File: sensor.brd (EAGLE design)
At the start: 30.5 x 35.6 mm, 17 parts, among them IC1 TINY261A

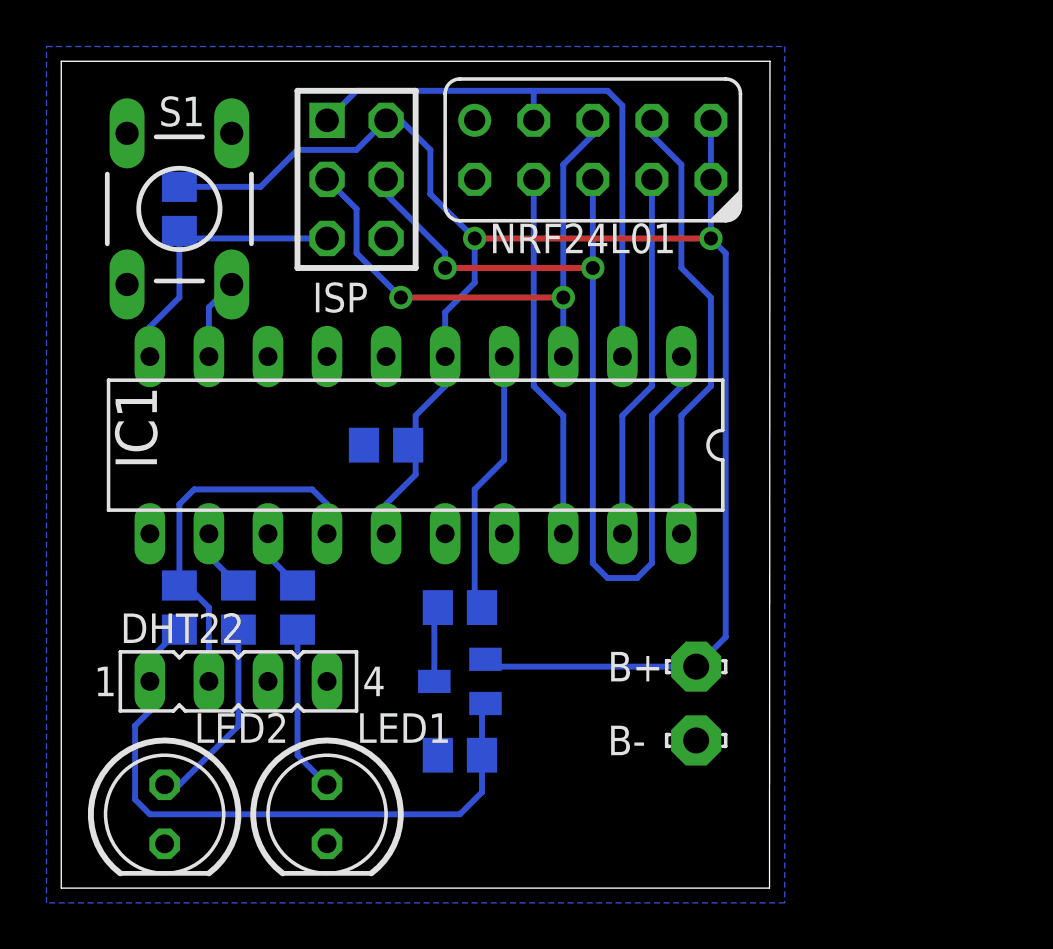
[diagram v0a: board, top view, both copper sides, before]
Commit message: added watch crystal to master, notes for sensor
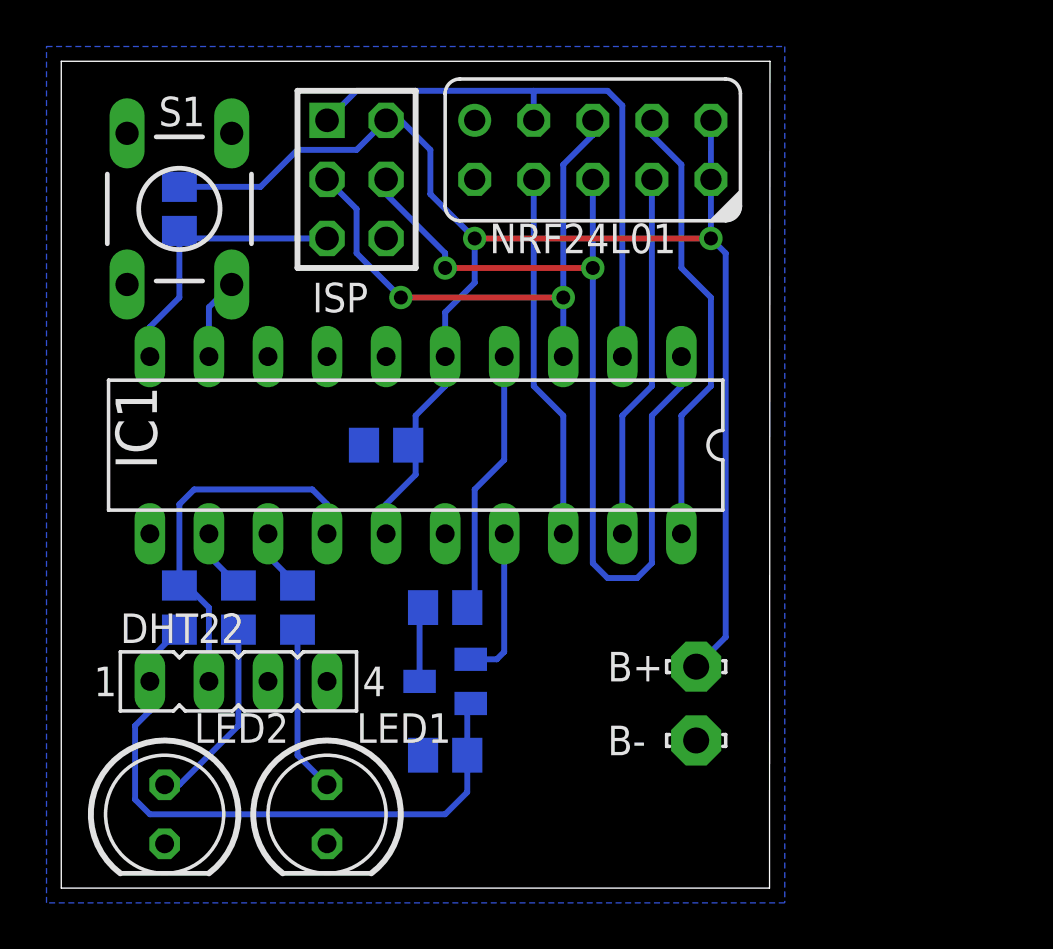
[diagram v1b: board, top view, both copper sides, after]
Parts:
- moved C2 0.63 mm to (16.5, 5.71)
- moved C3 0.63 mm to (16.5, 12.1)
- moved D1 0.63 mm to (16.5, 8.89)
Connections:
- new net PA3: D1.1, IC1.17
- net VCC: no longer D1.1
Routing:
- net VCC: track 75.3 -> 66.1 mm
- net PA3: track 0.00 -> 6.65 mm
- net DHTVCC: track 27.5 -> 26.9 mm
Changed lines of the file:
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@@
 <layer number="22" name="bPlace" color="7" fill="1" visible="yes" active="yes"/>
 <layer number="23" name="tOrigins" color="15" fill="1" visible="no" active="yes"/>
-<layer number="24" name="bOrigins" color="15" fill="1" visible="no" active="yes"/>
+<layer number="24" name="bOrigins" color="15" fill="1" visible="yes" active="yes"/>
 <layer number="25" name="tNames" color="7" fill="1" visible="yes" active="yes"/>
 <layer number="26" name="bNames" color="7" fill="1" visible="yes" active="yes"/>
@@
 <attribute name="VALUE" x="15.24" y="16.51" size="1.27" layer="28" rot="MR0"/>
 </element>
-<element name="C2" library="rcl" package="C0805" value="100n" x="17.145" y="5.715" smashed="yes" rot="MR180">
-<attribute name="NAME" x="19.05" y="6.35" size="1.27" layer="26" rot="MR180"/>
-<attribute name="VALUE" x="15.875" y="8.255" size="1.27" layer="28" rot="MR180"/>
+<element name="C2" library="rcl" package="C0805" value="100n" x="16.51" y="5.715" smashed="yes" rot="MR180">
+<attribute name="NAME" x="18.415" y="6.35" size="1.27" layer="26" rot="MR180"/>
+<attribute name="VALUE" x="15.24" y="8.255" size="1.27" layer="28" rot="MR180"/>
 </element>
 <element name="DHT22" library="con-lsta" package="FE04-1" value="" x="7.62" y="8.89"/>
 <element name="R2" library="rcl" package="R0805" value="10k" x="5.08" y="12.065" smashed="yes" rot="MR90">
-<attribute name="NAME" x="12.573" y="13.335" size="1.27" layer="26" rot="MR270"/>
+<attribute name="NAME" x="3.683" y="13.335" size="1.27" layer="26" rot="MR270"/>
 <attribute name="VALUE" x="2.54" y="11.43" size="1.27" layer="28" rot="MR90"/>
 </element>
@@
 <attribute name="VALUE" x="25.4" y="19.812" size="1.778" layer="27" ratio="10" rot="R180"/>
 </element>
-<element name="D1" library="diode" package="SOT23" value="BAT54S" x="17.145" y="8.89" smashed="yes" rot="MR270">
-<attribute name="NAME" x="19.05" y="8.89" size="1.27" layer="26" rot="MR180"/>
-<attribute name="VALUE" x="20.32" y="10.795" size="1.27" layer="28" rot="MR270"/>
-</element>
-<element name="C3" library="rcl" package="C0805" value="100n" x="17.145" y="12.065" smashed="yes" rot="MR0">
-<attribute name="NAME" x="19.05" y="12.7" size="1.27" layer="26" rot="MR180"/>
-<attribute name="VALUE" x="18.415" y="9.525" size="1.27" layer="28" rot="MR0"/>
+<element name="D1" library="diode" package="SOT23" value="BAT54S" x="16.51" y="8.89" smashed="yes" rot="MR270">
+<attribute name="NAME" x="18.415" y="8.89" size="1.27" layer="26" rot="MR180"/>
+<attribute name="VALUE" x="19.685" y="10.795" size="1.27" layer="28" rot="MR270"/>
+</element>
+<element name="C3" library="rcl" package="C0805" value="100n" x="16.51" y="12.065" smashed="yes" rot="MR0">
+<attribute name="NAME" x="18.415" y="12.7" size="1.27" layer="26" rot="MR180"/>
+<attribute name="VALUE" x="17.78" y="9.525" size="1.27" layer="28" rot="MR0"/>
 </element>
 <element name="R3" library="rcl" package="R0805" value="510" x="10.16" y="12.065" smashed="yes" rot="MR270">
-<attribute name="NAME" x="14.986" y="13.335" size="1.27" layer="26" rot="MR270"/>
+<attribute name="NAME" x="13.97" y="13.335" size="1.27" layer="26" rot="MR270"/>
 <attribute name="VALUE" x="12.7" y="12.7" size="1.27" layer="28" rot="MR270"/>
 </element>
@@
 </element>
 <element name="R4" library="rcl" package="R0805" value="470" x="7.62" y="12.065" smashed="yes" rot="MR270">
-<attribute name="NAME" x="13.716" y="13.335" size="1.27" layer="26" rot="MR270"/>
+<attribute name="NAME" x="12.7" y="13.335" size="1.27" layer="26" rot="MR270"/>
 <attribute name="VALUE" x="10.16" y="12.7" size="1.27" layer="28" rot="MR270"/>
 </element>
@@
 <contactref element="C1" pad="1"/>
 <wire x1="27.94" y1="30.48" x2="27.94" y2="33.02" width="0.254" layer="16"/>
-<contactref element="D1" pad="1"/>
 <wire x1="16.51" y1="22.86" x2="16.51" y2="24.765" width="0.254" layer="16"/>
 <wire x1="16.51" y1="24.765" x2="17.78" y2="26.035" width="0.254" layer="16"/>
@@
 <wire x1="27.94" y1="27.94" x2="28.575" y2="27.305" width="0.254" layer="16"/>
 <wire x1="28.575" y1="27.305" x2="28.575" y2="10.795" width="0.254" layer="16"/>
-<wire x1="27.305" y1="9.525" x2="18.56" y2="9.525" width="0.254" layer="16"/>
-<wire x1="18.56" y1="9.525" x2="18.245" y2="9.84" width="0.254" layer="16"/>
 <wire x1="28.575" y1="10.795" x2="27.305" y2="9.525" width="0.254" layer="16"/>
 <wire x1="15.24" y1="17.78" x2="13.97" y2="16.51" width="0.254" layer="16"/>
@@
 <wire x1="19.05" y1="22.86" x2="19.05" y2="18.415" width="0.254" layer="16"/>
 <wire x1="19.05" y1="18.415" x2="17.78" y2="17.145" width="0.254" layer="16"/>
-<wire x1="17.78" y1="17.145" x2="17.78" y2="12.38" width="0.254" layer="16"/>
-<wire x1="17.78" y1="12.38" x2="18.095" y2="12.065" width="0.254" layer="16"/>
+<wire x1="17.145" y1="12.38" x2="17.46" y2="12.065" width="0.254" layer="16"/>
+<wire x1="17.78" y1="17.145" x2="17.78" y2="12.385" width="0.254" layer="16"/>
+<wire x1="17.78" y1="12.385" x2="17.46" y2="12.065" width="0.254" layer="16"/>
 </signal>
 <signal name="PA2">
@@
 <contactref element="C3" pad="2"/>
 <contactref element="D1" pad="3"/>
-<wire x1="16.045" y1="8.89" x2="16.045" y2="11.915" width="0.254" layer="16"/>
-<wire x1="16.045" y1="11.915" x2="16.195" y2="12.065" width="0.254" layer="16"/>
+<wire x1="15.41" y1="8.89" x2="15.41" y2="11.915" width="0.254" layer="16"/>
+<wire x1="15.41" y1="11.915" x2="15.56" y2="12.065" width="0.254" layer="16"/>
 </signal>
 <signal name="DHTVCC">
@@
 <contactref element="C2" pad="2"/>
 <contactref element="R2" pad="1"/>
-<wire x1="18.095" y1="7.79" x2="18.245" y2="7.94" width="0.254" layer="16"/>
-<wire x1="18.095" y1="7.79" x2="18.095" y2="5.715" width="0.254" layer="16"/>
+<wire x1="17.46" y1="7.79" x2="17.61" y2="7.94" width="0.254" layer="16"/>
+<wire x1="17.46" y1="7.79" x2="17.46" y2="5.715" width="0.254" layer="16"/>
 <wire x1="3.81" y1="8.89" x2="3.81" y2="7.62" width="0.254" layer="16"/>
 <wire x1="3.81" y1="8.89" x2="3.81" y2="9.845" width="0.254" layer="16"/>
 <wire x1="3.81" y1="9.845" x2="5.08" y2="11.115" width="0.254" layer="16"/>
-<wire x1="18.095" y1="5.715" x2="18.095" y2="4.125" width="0.254" layer="16"/>
-<wire x1="18.095" y1="4.125" x2="17.145" y2="3.175" width="0.254" layer="16"/>
-<wire x1="17.145" y1="3.175" x2="3.81" y2="3.175" width="0.254" layer="16"/>
+<wire x1="17.46" y1="5.715" x2="17.46" y2="4.125" width="0.254" layer="16"/>
+<wire x1="17.46" y1="4.125" x2="16.51" y2="3.175" width="0.254" layer="16"/>
+<wire x1="16.51" y1="3.175" x2="3.81" y2="3.175" width="0.254" layer="16"/>
 <wire x1="3.81" y1="3.175" x2="3.175" y2="3.81" width="0.254" layer="16"/>
 <wire x1="3.175" y1="3.81" x2="3.175" y2="6.985" width="0.254" layer="16"/>
@@
 <wire x1="10.16" y1="5.715" x2="10.16" y2="11.115" width="0.254" layer="16"/>
 </signal>
+<signal name="PA3">
+<contactref element="IC1" pad="17"/>
+<contactref element="D1" pad="1"/>
+<wire x1="19.05" y1="15.24" x2="19.05" y2="10.16" width="0.254" layer="16"/>
+<wire x1="19.05" y1="10.16" x2="18.73" y2="9.84" width="0.254" layer="16"/>
+<wire x1="18.73" y1="9.84" x2="17.61" y2="9.84" width="0.254" layer="16"/>
+</signal>
 </signals>

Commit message: di == miso, do == mosi for usi in spi mode
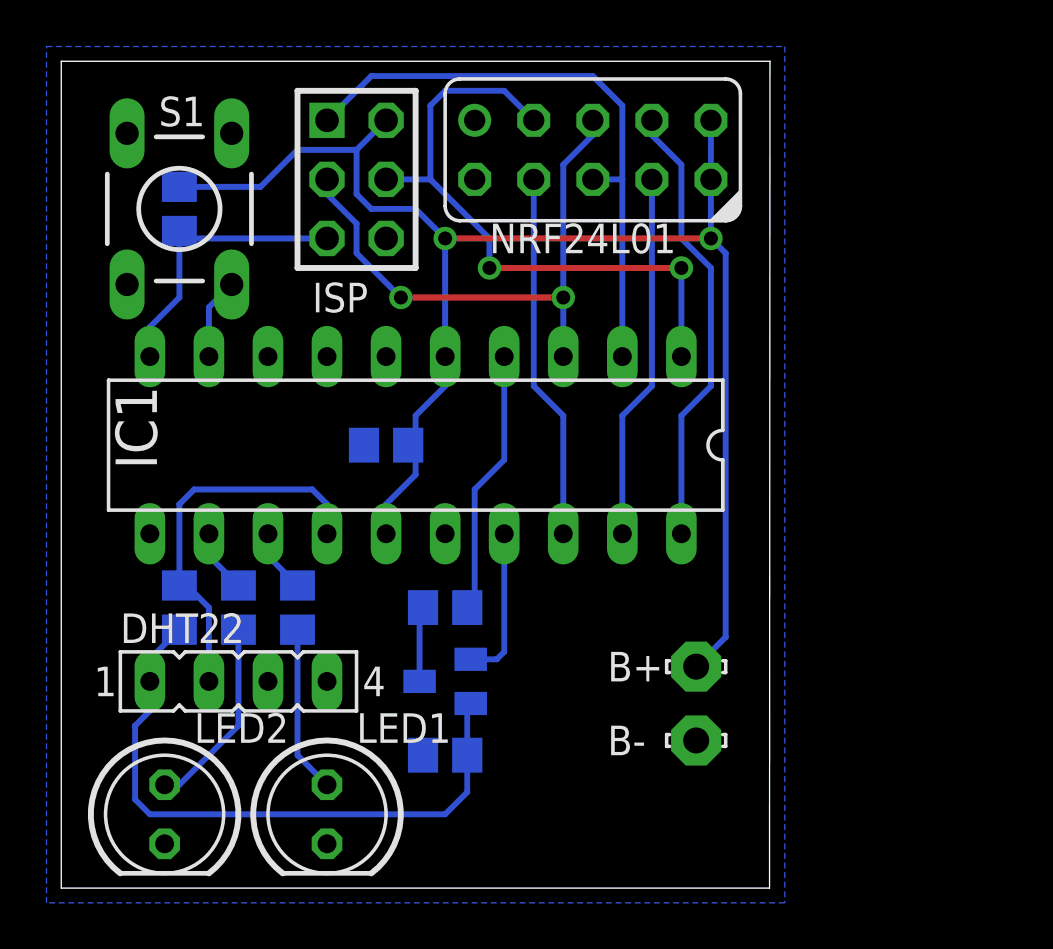
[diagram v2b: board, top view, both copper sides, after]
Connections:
- net PB0: now also NRF24L01.3; no longer NRF24L01.6
- net PB1: now also NRF24L01.6; no longer NRF24L01.3
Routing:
- net PB0: track 40.2 -> 27.2 mm
- net PB1: track 25.6 -> 26.1 mm
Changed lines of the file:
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@@
 <contactref element="C1" pad="1"/>
 <wire x1="27.94" y1="30.48" x2="27.94" y2="33.02" width="0.254" layer="16"/>
-<wire x1="16.51" y1="22.86" x2="16.51" y2="24.765" width="0.254" layer="16"/>
-<wire x1="16.51" y1="24.765" x2="17.78" y2="26.035" width="0.254" layer="16"/>
-<wire x1="17.78" y1="26.035" x2="17.78" y2="27.94" width="0.254" layer="16"/>
-<wire x1="17.78" y1="27.94" x2="15.875" y2="29.845" width="0.254" layer="16"/>
-<wire x1="15.875" y1="29.845" x2="15.875" y2="31.75" width="0.254" layer="16"/>
-<wire x1="15.875" y1="31.75" x2="14.605" y2="33.02" width="0.254" layer="16"/>
-<wire x1="14.605" y1="33.02" x2="13.97" y2="33.02" width="0.254" layer="16"/>
+<wire x1="16.51" y1="22.86" x2="16.51" y2="27.94" width="0.254" layer="16"/>
+<wire x1="12.7" y1="29.845" x2="12.7" y2="31.75" width="0.254" layer="16"/>
 <wire x1="5.08" y1="30.16" x2="8.57" y2="30.16" width="0.254" layer="16"/>
 <wire x1="8.57" y1="30.16" x2="10.16" y2="31.75" width="0.254" layer="16"/>
@@
 <wire x1="16.51" y1="21.59" x2="16.51" y2="22.86" width="0.254" layer="16"/>
 <wire x1="13.97" y1="15.24" x2="13.97" y2="16.51" width="0.254" layer="16"/>
-<via x="17.78" y="27.94" extent="1-16" drill="0.6"/>
-<wire x1="17.78" y1="27.94" x2="27.94" y2="27.94" width="0.254" layer="1"/>
+<via x="16.51" y="27.94" extent="1-16" drill="0.6"/>
+<wire x1="16.51" y1="27.94" x2="27.94" y2="27.94" width="0.254" layer="1"/>
 <via x="27.94" y="27.94" extent="1-16" drill="0.6"/>
 <wire x1="27.94" y1="27.94" x2="27.94" y2="30.48" width="0.254" layer="16"/>
@@
 <wire x1="15.24" y1="20.32" x2="15.24" y2="19.37" width="0.254" layer="16"/>
 <wire x1="15.24" y1="19.37" x2="14.92" y2="19.05" width="0.254" layer="16"/>
+<wire x1="12.7" y1="29.845" x2="13.335" y2="29.21" width="0.254" layer="16"/>
+<wire x1="13.335" y1="29.21" x2="15.24" y2="29.21" width="0.254" layer="16"/>
+<wire x1="15.24" y1="29.21" x2="16.51" y2="27.94" width="0.254" layer="16"/>
 </signal>
 <signal name="PA4">
@@
 </signal>
 <signal name="PB0">
-<contactref element="NRF24L01" pad="6"/>
 <contactref element="ISP" pad="4"/>
 <contactref element="IC1" pad="1"/>
-<wire x1="13.97" y1="30.48" x2="13.97" y2="29.845" width="0.254" layer="16"/>
-<wire x1="13.97" y1="29.845" x2="16.51" y2="27.305" width="0.254" layer="16"/>
-<wire x1="16.51" y1="27.305" x2="16.51" y2="26.67" width="0.254" layer="16"/>
-<wire x1="26.67" y1="22.86" x2="26.67" y2="21.59" width="0.254" layer="16"/>
-<wire x1="26.67" y1="21.59" x2="25.4" y2="20.32" width="0.254" layer="16"/>
-<wire x1="25.4" y1="20.32" x2="25.4" y2="13.97" width="0.254" layer="16"/>
-<wire x1="25.4" y1="13.97" x2="24.765" y2="13.335" width="0.254" layer="16"/>
-<wire x1="24.765" y1="13.335" x2="23.495" y2="13.335" width="0.254" layer="16"/>
-<wire x1="23.495" y1="13.335" x2="22.86" y2="13.97" width="0.254" layer="16"/>
-<wire x1="22.86" y1="26.67" x2="22.86" y2="13.97" width="0.254" layer="16"/>
-<via x="16.51" y="26.67" extent="1-16" drill="0.6"/>
-<wire x1="16.51" y1="26.67" x2="22.86" y2="26.67" width="0.254" layer="1"/>
-<via x="22.86" y="26.67" extent="1-16" drill="0.6"/>
-<wire x1="22.86" y1="26.67" x2="22.86" y2="30.48" width="0.254" layer="16"/>
+<wire x1="15.875" y1="30.48" x2="18.415" y2="27.94" width="0.254" layer="16"/>
+<wire x1="18.415" y1="27.94" x2="18.415" y2="26.67" width="0.254" layer="16"/>
+<wire x1="26.67" y1="26.67" x2="26.67" y2="22.86" width="0.254" layer="16"/>
+<via x="18.415" y="26.67" extent="1-16" drill="0.6"/>
+<wire x1="18.415" y1="26.67" x2="26.67" y2="26.67" width="0.254" layer="1"/>
+<via x="26.67" y="26.67" extent="1-16" drill="0.6"/>
+<contactref element="NRF24L01" pad="3"/>
+<wire x1="20.32" y1="33.02" x2="19.05" y2="34.29" width="0.254" layer="16"/>
+<wire x1="19.05" y1="34.29" x2="16.51" y2="34.29" width="0.254" layer="16"/>
+<wire x1="16.51" y1="34.29" x2="15.875" y2="33.655" width="0.254" layer="16"/>
+<wire x1="15.875" y1="33.655" x2="15.875" y2="30.48" width="0.254" layer="16"/>
+<wire x1="15.875" y1="30.48" x2="13.97" y2="30.48" width="0.254" layer="16"/>
 </signal>
 <signal name="PB1">
-<contactref element="NRF24L01" pad="3"/>
 <contactref element="ISP" pad="1"/>
 <contactref element="IC1" pad="2"/>
-<wire x1="24.13" y1="22.86" x2="24.13" y2="33.655" width="0.254" layer="16"/>
-<wire x1="24.13" y1="33.655" x2="23.495" y2="34.29" width="0.254" layer="16"/>
-<wire x1="23.495" y1="34.29" x2="20.32" y2="34.29" width="0.254" layer="16"/>
-<wire x1="11.43" y1="33.02" x2="12.7" y2="34.29" width="0.254" layer="16"/>
-<wire x1="12.7" y1="34.29" x2="20.32" y2="34.29" width="0.254" layer="16"/>
-<wire x1="20.32" y1="34.29" x2="20.32" y2="33.02" width="0.254" layer="16"/>
+<wire x1="24.13" y1="22.86" x2="24.13" y2="30.48" width="0.254" layer="16"/>
+<contactref element="NRF24L01" pad="6"/>
+<wire x1="22.86" y1="30.48" x2="24.13" y2="30.48" width="0.254" layer="16"/>
+<wire x1="24.13" y1="30.48" x2="24.13" y2="33.655" width="0.254" layer="16"/>
+<wire x1="24.13" y1="33.655" x2="22.86" y2="34.925" width="0.254" layer="16"/>
+<wire x1="22.86" y1="34.925" x2="13.335" y2="34.925" width="0.254" layer="16"/>
+<wire x1="13.335" y1="34.925" x2="11.43" y2="33.02" width="0.254" layer="16"/>
 </signal>
 <signal name="PB2">
@@
 <wire x1="21.59" y1="31.115" x2="21.59" y2="25.4" width="0.254" layer="16"/>
 <wire x1="21.59" y1="25.4" x2="21.59" y2="22.86" width="0.254" layer="16"/>
-<wire x1="11.43" y1="30.48" x2="12.7" y2="29.21" width="0.254" layer="16"/>
-<wire x1="12.7" y1="29.21" x2="12.7" y2="27.305" width="0.254" layer="16"/>
+<wire x1="11.43" y1="30.48" x2="11.43" y2="29.845" width="0.254" layer="16"/>
+<wire x1="11.43" y1="29.845" x2="12.7" y2="28.575" width="0.254" layer="16"/>
+<wire x1="12.7" y1="28.575" x2="12.7" y2="27.305" width="0.254" layer="16"/>
 <wire x1="12.7" y1="27.305" x2="14.605" y2="25.4" width="0.254" layer="16"/>
 <via x="14.605" y="25.4" extent="1-16" drill="0.6"/>
@@
 <wire x1="26.67" y1="15.24" x2="26.67" y2="20.32" width="0.254" layer="16"/>
 <wire x1="26.67" y1="20.32" x2="27.94" y2="21.59" width="0.254" layer="16"/>
-<wire x1="27.94" y1="21.59" x2="27.94" y2="25.4" width="0.254" layer="16"/>
-<wire x1="27.94" y1="25.4" x2="26.67" y2="26.67" width="0.254" layer="16"/>
-<wire x1="26.67" y1="26.67" x2="26.67" y2="31.115" width="0.254" layer="16"/>
+<wire x1="27.94" y1="21.59" x2="27.94" y2="26.67" width="0.254" layer="16"/>
+<wire x1="27.94" y1="26.67" x2="26.67" y2="27.94" width="0.254" layer="16"/>
+<wire x1="26.67" y1="27.94" x2="26.67" y2="31.115" width="0.254" layer="16"/>
 <wire x1="26.67" y1="31.115" x2="25.4" y2="32.385" width="0.254" layer="16"/>
 <wire x1="25.4" y1="32.385" x2="25.4" y2="33.02" width="0.254" layer="16"/>
